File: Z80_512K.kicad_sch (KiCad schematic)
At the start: 24 parts, among them J1 USB_B_Mini, J2 EXPANSION-BUS, SW1 ON|OFF, SW2 Z80_RESET, U1 Z84C00/PLCC, U2 74HCT574, U3 AS6C4008-55PCN, U4 74HC138, U5 SST39SF040, U6 74HC74, U7 74HC00, Y1 CXO_DIP14

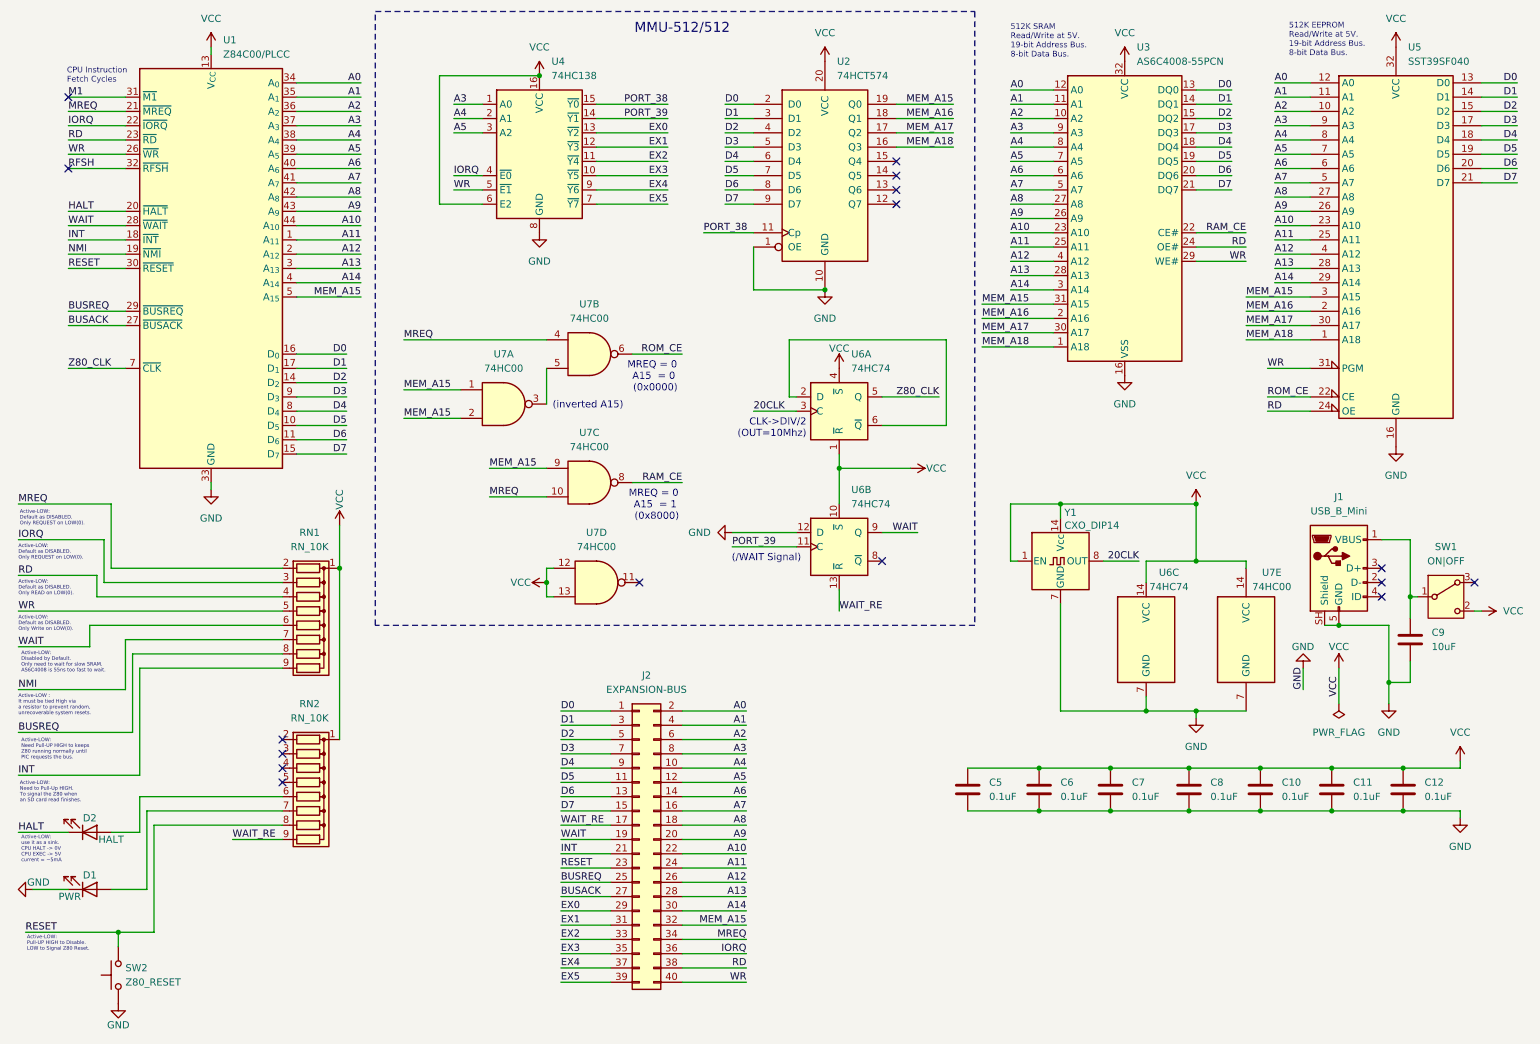
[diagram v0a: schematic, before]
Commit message: Finished Routing Layout.
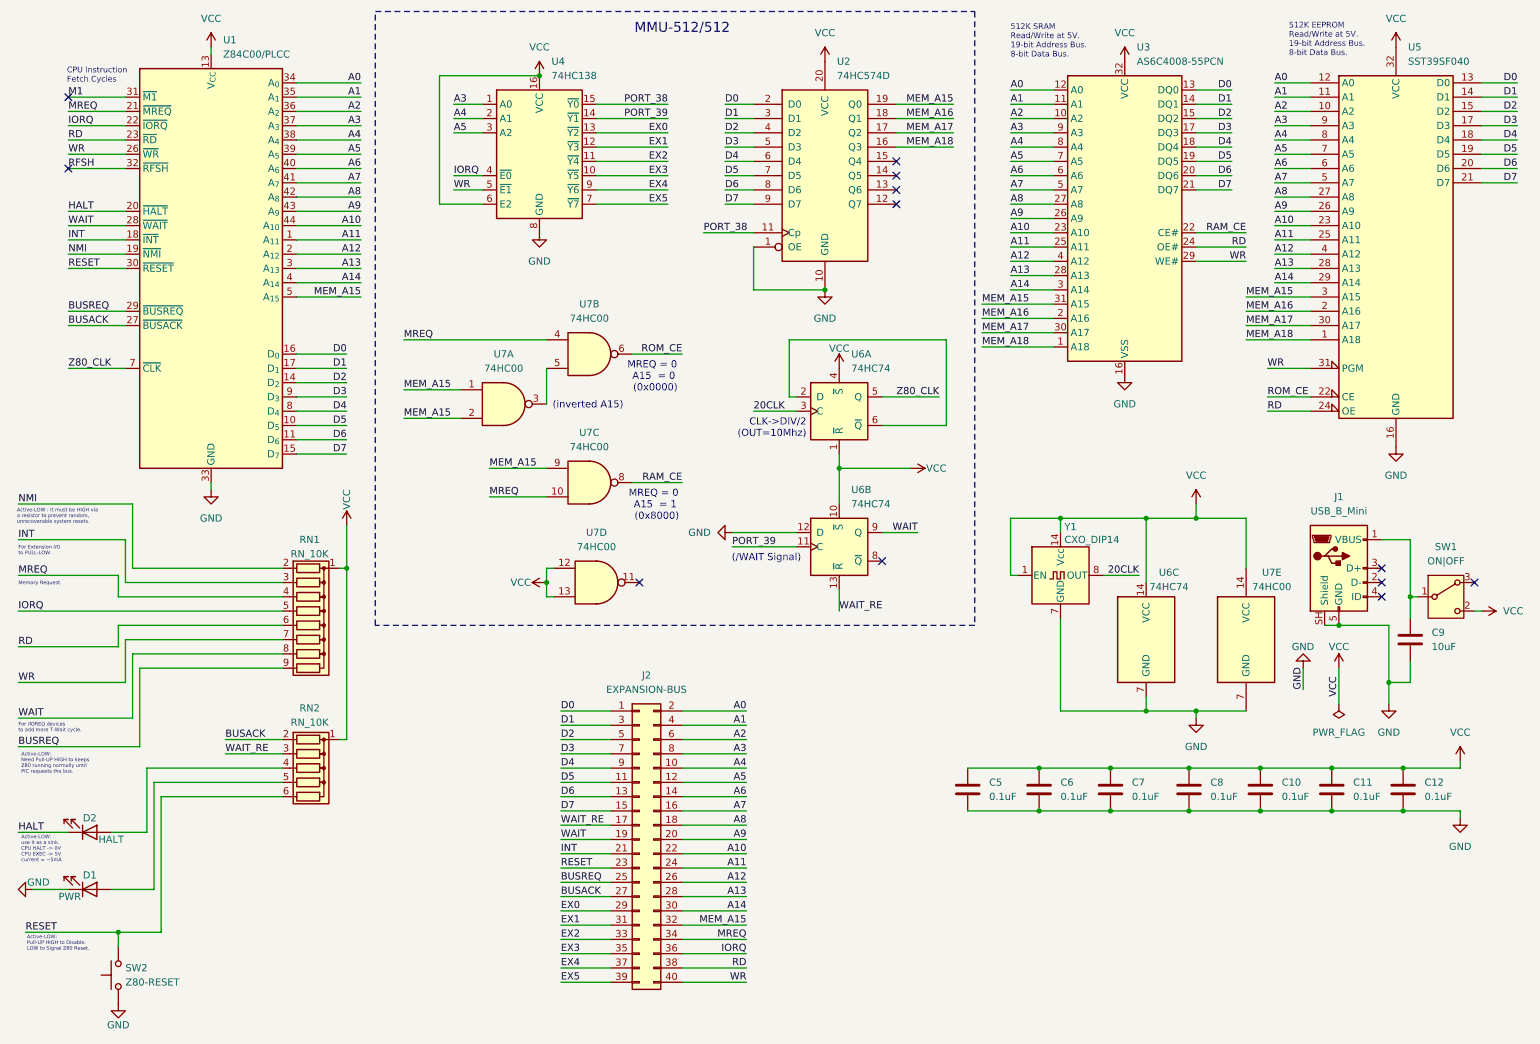
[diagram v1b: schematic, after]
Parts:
- removed RN2: RN_10K, Resistor_THT:R_Array_SIP9, symbol Device:R_Network08
- added RN2: RN_10K, Resistor_THT:R_Array_SIP6, symbol Device:R_Network05
- SW2: value Z80_RESET -> Z80-RESET
- U2: value 74HCT574 -> 74HC574D; footprint Package_SO:SOP-20_7.5x12.8mm_P1.27mm -> Package_DIP:DIP-20_W7.62mm
- U3: footprint Package_SO:SOP-32_11.305x20.495mm_P1.27mm -> Package_DIP:DIP-32_W15.24mm
- U4: footprint Package_SO:SOIC-16_3.9x9.9mm_P1.27mm -> Package_DIP:DIP-16_W7.62mm
- U5: footprint Package_LCC:PLCC-32_THT-Socket -> Package_DIP:DIP-32_W15.24mm
- U6, U7: footprint Package_SO:SOIC-14_3.9x8.7mm_P1.27mm -> Package_DIP:DIP-14_W10.16mm
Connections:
- net BUSACK: now also RN2.2 (R1)
- net BUSREQ: now also RN1.9 (R8); no longer RN1.8 (R7)
- net INT: now also RN1.3 (R2); no longer RN1.9 (R8)
- net IORQ: now also RN1.5 (R4); no longer RN1.3 (R2)
- net MREQ: now also RN1.4 (R3); no longer RN1.2 (R1)
- net NMI: now also RN1.2 (R1); no longer RN1.7 (R6)
- net RD: now also RN1.6 (R5); no longer RN1.4 (R3)
- net RESET: now also RN2.6 (R5)
- net VCC: now also RN2.1 (common)
- net WAIT: now also RN1.8 (R7); no longer RN1.6 (R5)
- net WAIT_RE: now also RN2.3 (R2)
- net WR: now also RN1.7 (R6); no longer RN1.5 (R4)
- net at D1.2 (A): now also RN2.5 (R4)
- net at D2.2 (A): now also RN2.4 (R3)
- no-connect marks 16 -> 12
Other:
- note added: "Active-LOW : It must be HIGH via a resistor to prevent random, unrecoverable system resets."
- note added: "For /IOREQ devices to add more T-Wait cycle."
- note added: "For Extension I/O to PULL-LOW."
- note added: "Memory Request."
- note removed: "Active-LOW : It must be tied High via a resistor to prevent random, unrecoverable system resets."
- note removed: "Active-LOW: Default as DISABLED. Only READ on LOW(0)."
- note removed: "Active-LOW: Default as DISABLED. Only REQUEST on LOW(0)."
- note removed: "Active-LOW: Default as DISABLED. Only Write on LOW(0)."
- note removed: "Active-LOW: Disabled by Default. Only need to wait for slow SRAM. AS6C4008 is 55ns too fast to wait."
- note removed: "Active-LOW: Need to Pull-Up HIGH. To signal the Z80 when an SD card read finishes."
- moved on the sheet: Y1

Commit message: RN-A06 ~> RN-A05: remove R-BUSACK
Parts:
- removed RN2: RN_10K, Resistor_THT:R_Array_SIP6, symbol Device:R_Network05
- added RN2: RN_10K, Resistor_THT:R_Array_SIP5, symbol Device:R_Network04
- U2: value 74HC574D -> 74HC574
- U3: value AS6C4008-55PCN -> 512K-SRAM
- U5: value SST39SF040 -> 512K-EEPROM
- Y1: value CXO_DIP14 -> 20MHz-DIP14
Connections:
- net RESET: now also RN2.5 (R4)
- net VCC: now also RN2.1 (common)
- net WAIT_RE: now also RN2.2 (R1)
- net at D1.2 (A): now also RN2.4 (R3)
- net at D2.2 (A): now also RN2.3 (R2)
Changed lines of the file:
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@@
 	)
 	(junction
-		(at 199.39 104.14)
-		(diameter 0)
-		(color 0 0 0 0)
-	)
-	(junction
 		(at 260.35 156.21)
 		(diameter 0)
@@
 	)
 	(junction
+		(at 199.39 104.14)
+		(diameter 0)
+		(color 0 0 0 0)
+	)
+	(junction
 		(at 31.75 177.8)
 		(diameter 0)
@@
 	(wire
 		(pts
-			(xy 50.8 143.51) (xy 60.96 143.51)
-		)
-		(stroke
-			(width 0)
-			(type default)
-		)
-	)
-	(wire
-		(pts
 			(xy 22.86 52.07) (xy 33.02 52.07)
 		)
@@
 	(wire
 		(pts
-			(xy 72.39 143.51) (xy 72.39 113.03)
+			(xy 72.39 146.05) (xy 72.39 113.03)
 		)
 		(stroke
@@
 	(wire
 		(pts
-			(xy 71.12 143.51) (xy 72.39 143.51)
+			(xy 71.12 146.05) (xy 72.39 146.05)
 		)
 		(stroke
@@
 		)
 	)
-	(label "BUSACK"
-		(at 50.8 143.51 0)
-		(effects
-			(font
-				(size 1.27 1.27)
-			)
-			(justify left bottom)
-		)
-	)
 	(label "INT"
 		(at 13.97 107.95 0)
@@
 			)
 		)
-		(property "Value" "SST39SF040"
+		(property "Value" "512K-EEPROM"
 			(at 261.2233 22.86 0)
 			(show_name no)
@@
 	)
 	(symbol
+		(lib_id "Device:R_Network04")
+		(at 66.04 151.13 270)
+		(unit 1)
+		(body_style 1)
+		(exclude_from_sim no)
+		(in_bom yes)
+		(on_board yes)
+		(in_pos_files yes)
+		(dnp no)
+		(property "Reference" "RN2"
+			(at 65.786 140.462 90)
+			(show_name no)
+			(do_not_autoplace no)
+			(effects
+				(font
+					(size 1.27 1.27)
+				)
+			)
+		)
+		(property "Value" "RN_10K"
+			(at 65.786 143.002 90)
+			(show_name no)
+			(do_not_autoplace no)
+			(effects
+				(font
+					(size 1.27 1.27)
+				)
+			)
+		)
+		(property "Footprint" "Resistor_THT:R_Array_SIP5"
+			(at 66.04 158.115 90)
+			(hide yes)
+			(show_name no)
+			(do_not_autoplace no)
+			(effects
+				(font
+					(size 1.27 1.27)
+				)
+			)
+		)
+		(property "Datasheet" "http://www.vishay.com/docs/31509/csc.pdf"
+			(at 66.04 151.13 0)
+			(hide yes)
+			(show_name no)
+			(do_not_autoplace no)
+			(effects
+				(font
+					(size 1.27 1.27)
+				)
+			)
+		)
+		(property "Description" "4 resistor network, star topology, bussed resistors, small symbol"
+			(at 66.04 151.13 0)
+			(hide yes)
+			(show_name no)
+			(do_not_autoplace no)
+			(effects
+				(font
+					(size 1.27 1.27)
+				)
+			)
+		)
+		(pin "1"
+		)
+		(pin "2"
+		)
+		(pin "3"
+		)
+		(pin "4"
+		)
+		(pin "5"
+		)
+		(instances
+			(project "Z80_512K"
+				(path "/1dee2e6f-8929-455d-a1de-5fd790cf69ac"
+					(reference "RN2")
+					(unit 1)
+				)
+			)
+		)
+	)
+	(symbol
 		(lib_id "power:GND")
 		(at 140.97 106.68 270)
@@
 			)
 		)
-		(property "Value" "74HC574D"
+		(property "Value" "74HC574"
 			(at 159.6233 25.4 0)
 			(show_name no)
@@
 			)
 		)
-		(property "Value" "AS6C4008-55PCN"
+		(property "Value" "512K-SRAM"
 			(at 212.9633 22.86 0)
 			(show_name no)
@@
 			)
 		)
-		(property "Value" "CXO_DIP14"
-			(at 204.978 107.95 0)
+		(property "Value" "20MHz-DIP14"
+			(at 206.502 107.95 0)
 			(show_name no)
 			(do_not_autoplace no)
@@
 					(unit 1)
 				)
-			)
-		)
-	)
-	(symbol
-		(lib_id "Device:R_Network05")
-		(at 66.04 148.59 270)
-		(unit 1)
-		(body_style 1)
-		(exclude_from_sim no)
-		(in_bom yes)
-		(on_board yes)
-		(in_pos_files yes)
-		(dnp no)
-		(property "Reference" "RN2"
-			(at 65.786 137.922 90)
-			(show_name no)
-			(do_not_autoplace no)
-			(effects
-				(font
-					(size 1.27 1.27)
-				)
-			)
-		)
-		(property "Value" "RN_10K"
-			(at 65.786 140.462 90)
-			(show_name no)
-			(do_not_autoplace no)
-			(effects
-				(font
-					(size 1.27 1.27)
-				)
-			)
-		)
-		(property "Footprint" "Resistor_THT:R_Array_SIP6"
-			(at 66.04 158.115 90)
-			(hide yes)
-			(show_name no)
-			(do_not_autoplace no)
-			(effects
-				(font
-					(size 1.27 1.27)
-				)
-			)
-		)
-		(property "Datasheet" "http://www.vishay.com/docs/31509/csc.pdf"
-			(at 66.04 148.59 0)
-			(hide yes)
-			(show_name no)
-			(do_not_autoplace no)
-			(effects
-				(font
-					(size 1.27 1.27)
-				)
-			)
-		)
-		(property "Description" "5 resistor network, star topology, bussed resistors, small symbol"
-			(at 66.04 148.59 0)
-			(hide yes)
-			(show_name no)
-			(do_not_autoplace no)
-			(effects
-				(font
-					(size 1.27 1.27)
-				)
-			)
-		)
-		(pin "1"
-		)
-		(pin "2"
-		)
-		(pin "3"
-		)
-		(pin "4"
-		)
-		(pin "5"
-		)
-		(pin "6"
-		)
-		(instances
-			(project "Z80_512K"
-				(path "/1dee2e6f-8929-455d-a1de-5fd790cf69ac"
-					(reference "RN2")
-					(unit 1)
-				)

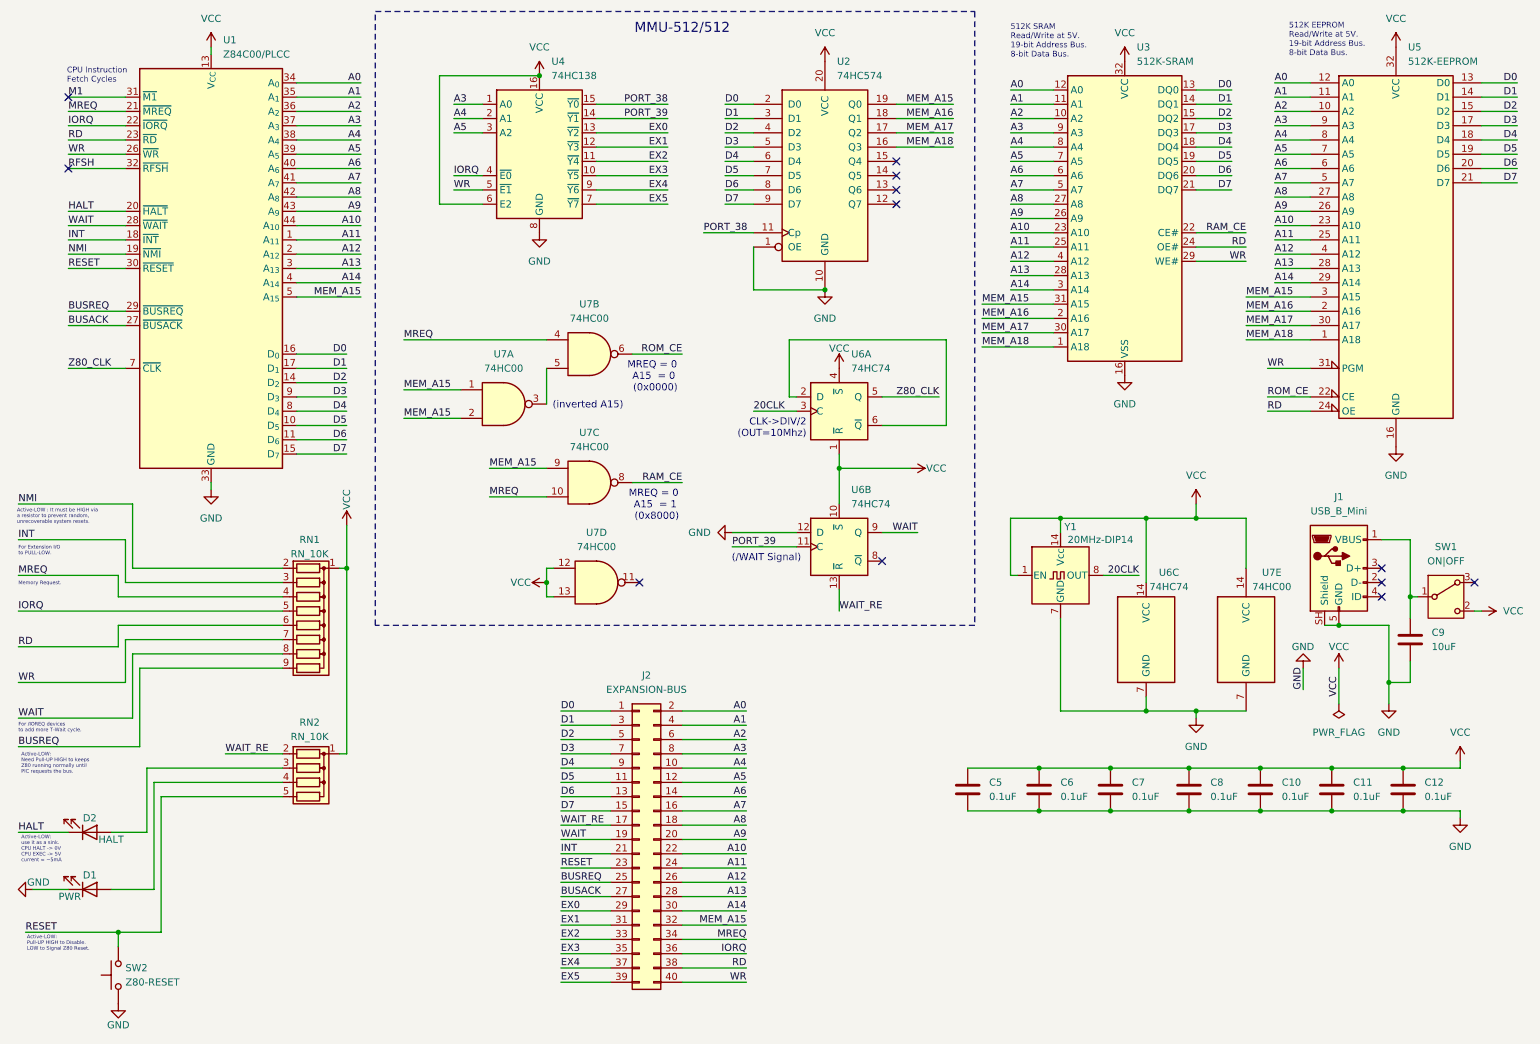
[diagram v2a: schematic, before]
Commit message: Refine Expansion-Bus: remove all EXs & add VCC/GND rails + Diode/USB.
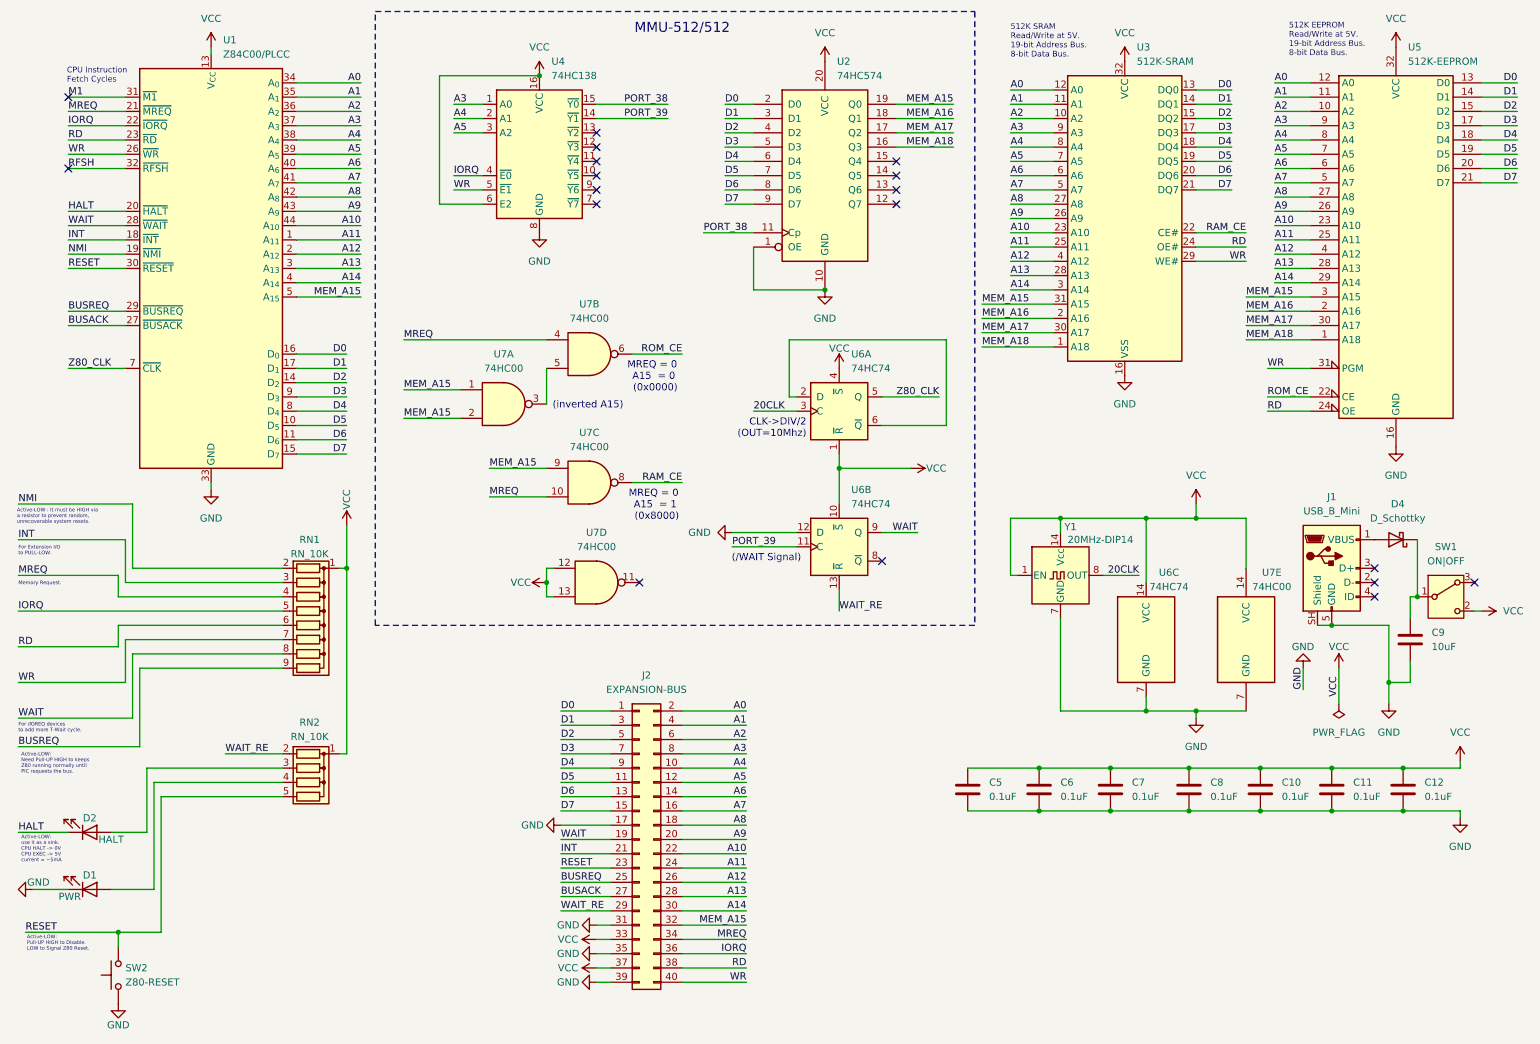
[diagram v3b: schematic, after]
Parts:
- added D4: D_Schottky, Diode_THT:D_DO-41_SOD81_P10.16mm_Horizontal, symbol Device:D_Schottky
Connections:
- net GND: now also J2.17 (Pin_17), J2.31 (Pin_31), J2.35 (Pin_35), J2.39 (Pin_39)
- net VCC: now also J2.33 (Pin_33), J2.37 (Pin_37)
- net WAIT_RE: now also J2.29 (Pin_29); no longer J2.17 (Pin_17)
- net at C9.2, SW1.1 (B): now also D4.1 (K); no longer J1.1 (VBUS)
- net EX0: no longer names the net of U4.13 (~{Y2})
- net EX0: no longer J2.29 (Pin_29)
- net EX1: no longer names the net of U4.12 (~{Y3})
- net EX1: no longer J2.31 (Pin_31)
- net EX2: no longer names the net of U4.11 (~{Y4})
- net EX2: no longer J2.33 (Pin_33)
- net EX3: no longer names the net of U4.10 (~{Y5})
- net EX3: no longer J2.35 (Pin_35)
- net EX4: no longer names the net of U4.9 (~{Y6})
- net EX4: no longer J2.37 (Pin_37)
- net EX5: no longer names the net of U4.7 (~{Y7})
- net EX5: no longer J2.39 (Pin_39)
- new net: D4.2 (A), J1.1 (VBUS)
- no-connect marks 12 -> 18
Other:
- moved on the sheet: J1
